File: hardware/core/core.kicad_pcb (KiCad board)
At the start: 4 copper layers, 31.3 x 67.7 mm, 32 parts, among them J17 PROG, J18 USB_C_Receptacle_USB2.0_14P, J5 TO_NEXT, J7 TO_NEXT, J8 Conn_02x09_Odd_Even, SW1 RESET, SW2 BOOT, U10 SN74AHCT1G14DCKR, U19 ESP32-S3-MINI-1, U20 AP2112K-3.3TRG1, U21 SN65HVD230DR

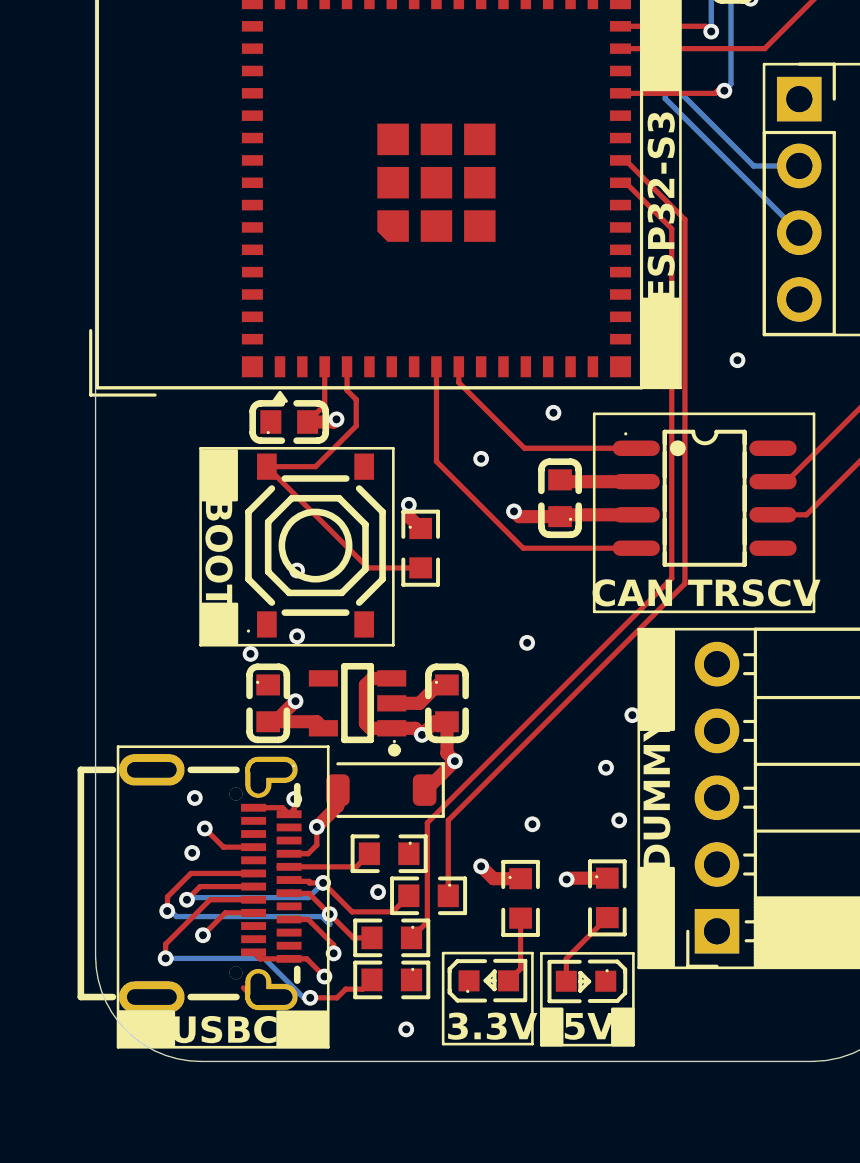
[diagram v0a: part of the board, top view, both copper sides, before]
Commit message: changed schottky with a ss54 and reduced VBUS route length
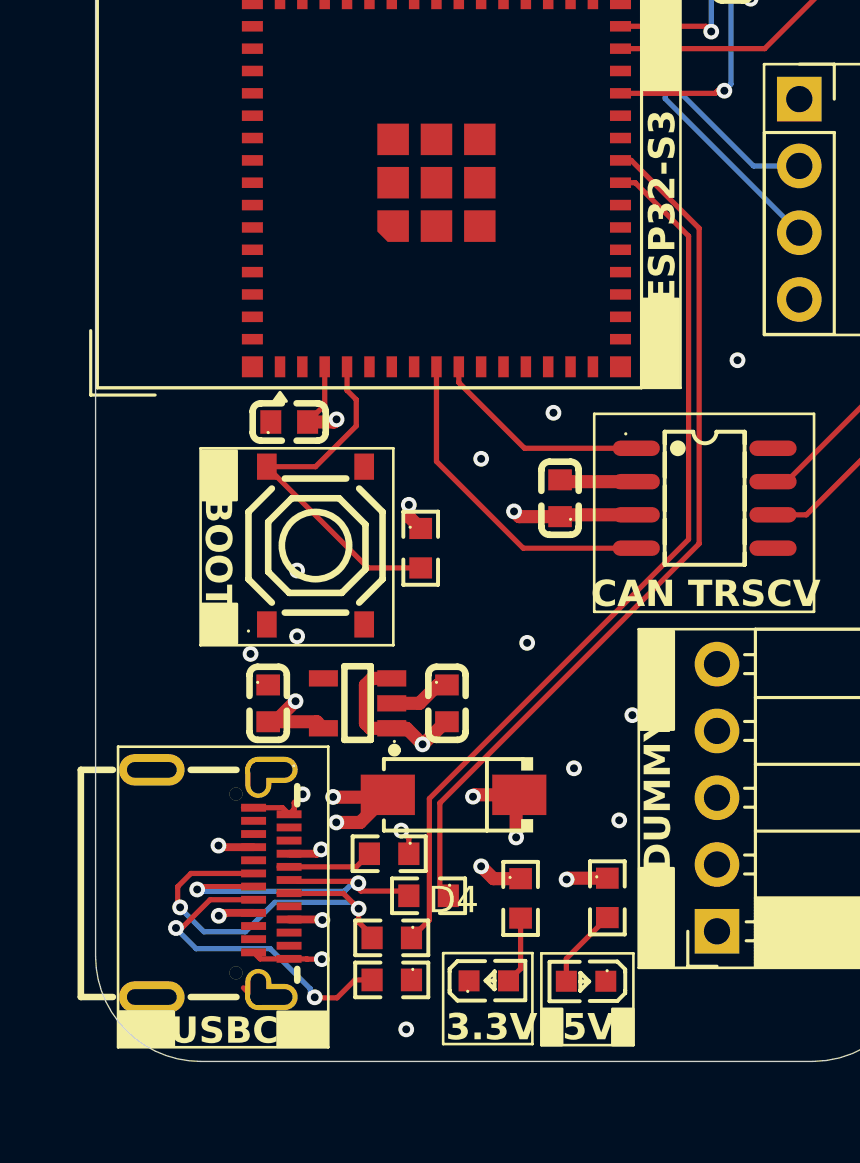
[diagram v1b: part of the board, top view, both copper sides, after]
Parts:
- removed D1: MBR0520LT1G, Diode_SMD:D_SOD-123
- added D4: SS54_C22452, SpaghettiLAB:SMA_L4.4-W2.8-LS5.4-R-RD, F.Cu at (80.7, 125.3)
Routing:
- net Net-(J18-D--PadA7): track 14.9 -> 15.9 mm
- net Net-(J18-CC2): track 13.0 -> 12.0 mm
- net GND: track 13.1 -> 14.1 mm, vias 26 -> 23
- net USB_D+: track 32.8 -> 33.7 mm
- net USB_D-: track 33.7 -> 34.5 mm
- net 5V: track 22.1 -> 22.4 mm, vias 5 -> 6
- net VBUS: track 10.5 -> 10.3 mm, vias 4 -> 6

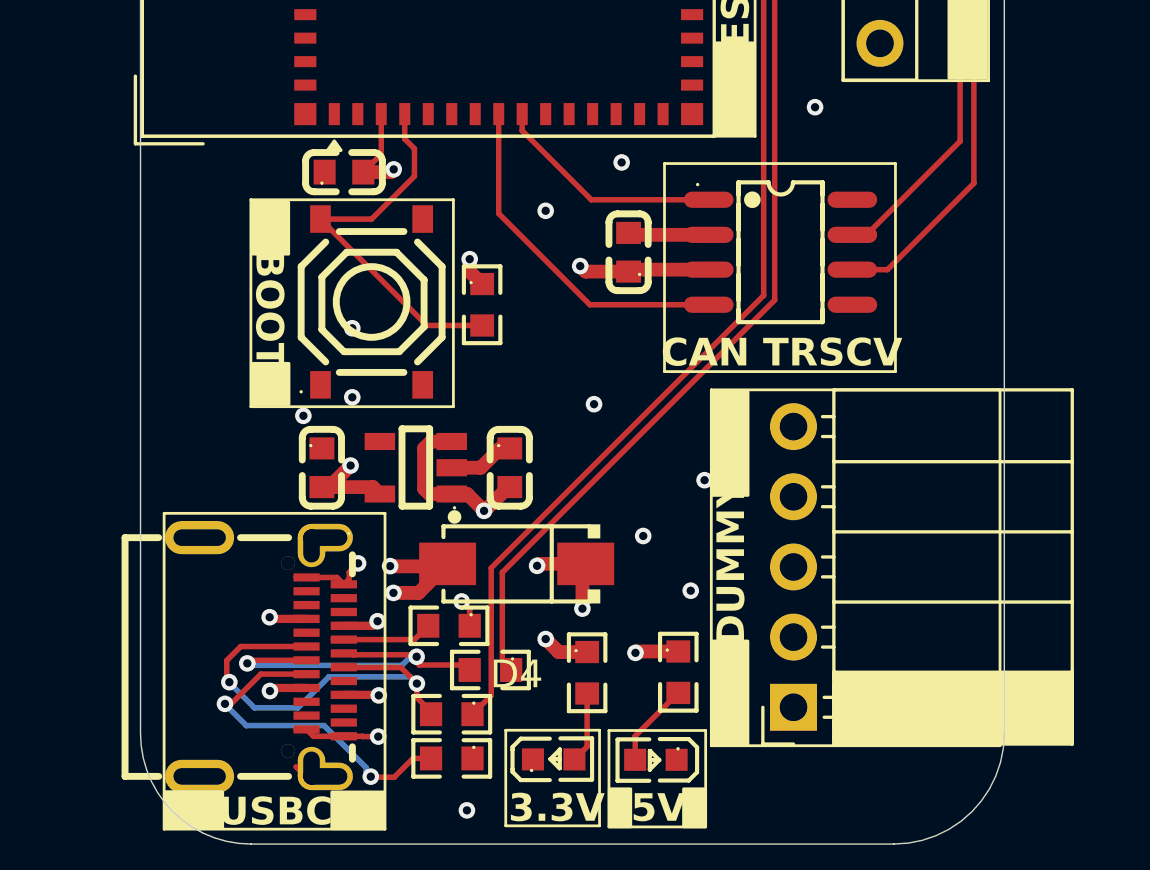
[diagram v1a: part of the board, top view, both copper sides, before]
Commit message: minor fixes to silkscreen, added rev a
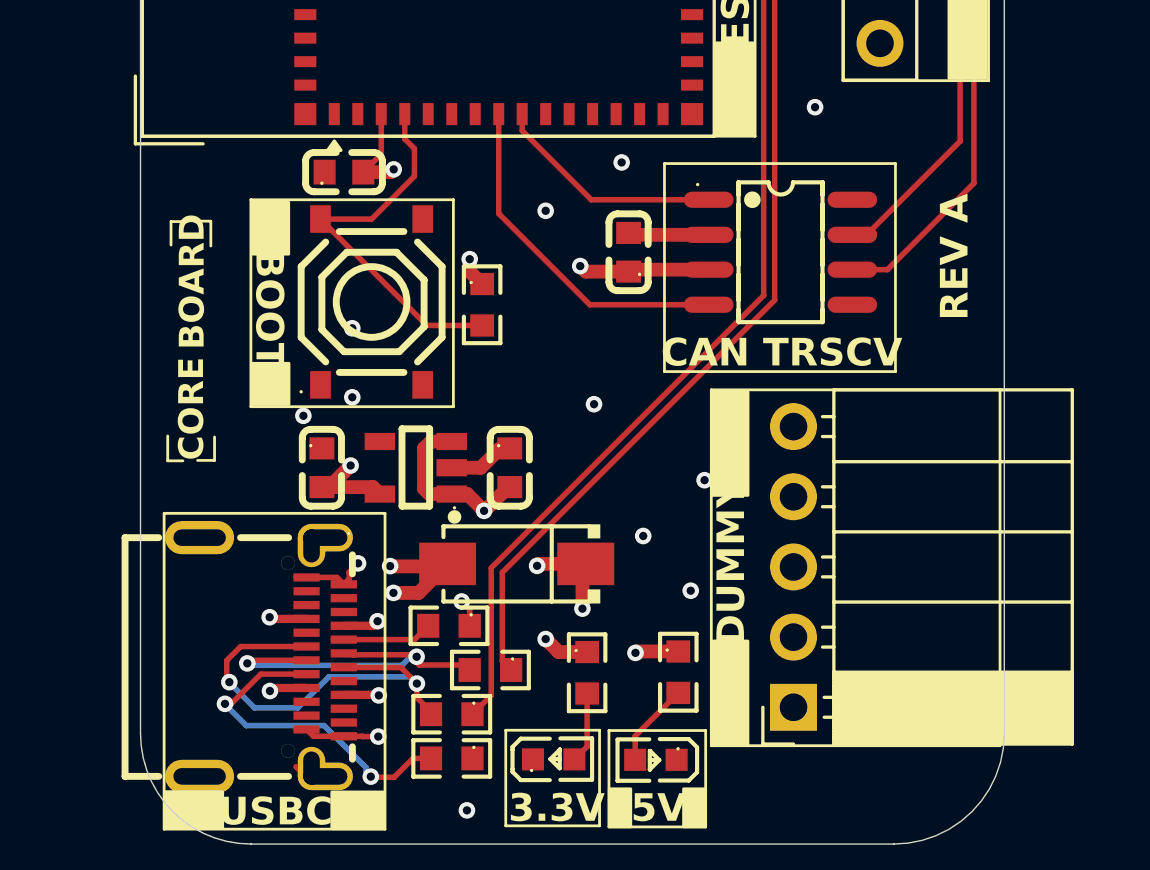
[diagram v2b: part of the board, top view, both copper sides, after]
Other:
- board text added: "BOARD"
- board text added: "CORE"
- board text added: "REV A"
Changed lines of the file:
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@@
 			(at 0 -4 0)
 			(layer "F.SilkS")
+			(hide yes)
 			(effects
 				(font
@@
 				(font
 					(size 1.27 1.27)
+					(thickness 0.15)
 				)
 			)
@@
 		(layer "F.SilkS")
 	)
+	(gr_line
+		(start 68.07 121.55)
+		(end 68.07 120.65)
+		(stroke
+			(width 0.1)
+			(type default)
+		)
+		(layer "F.SilkS")
+	)
+	(gr_line
+		(start 68.19 112.89)
+		(end 68.74 112.89)
+		(stroke
+			(width 0.1)
+			(type default)
+		)
+		(layer "F.SilkS")
+	)
+	(gr_line
+		(start 68.19 113.74)
+		(end 68.19 112.89)
+		(stroke
+			(width 0.1)
+			(type default)
+		)
+		(layer "F.SilkS")
+	)
+	(gr_line
+		(start 68.62 121.55)
+		(end 68.07 121.55)
+		(stroke
+			(width 0.1)
+			(type default)
+		)
+		(layer "F.SilkS")
+	)
+	(gr_line
+		(start 69.08 112.875)
+		(end 69.63 112.875)
+		(stroke
+			(width 0.1)
+			(type default)
+		)
+		(layer "F.SilkS")
+	)
+	(gr_line
+		(start 69.63 112.875)
+		(end 69.63 113.775)
+		(stroke
+			(width 0.1)
+			(type default)
+		)
+		(layer "F.SilkS")
+	)
+	(gr_line
+		(start 69.765 120.685)
+		(end 69.765 121.535)
+		(stroke
+			(width 0.1)
+			(type default)
+		)
+		(layer "F.SilkS")
+	)
+	(gr_line
+		(start 69.765 121.535)
+		(end 69.15 121.535)
+		(stroke
+			(width 0.1)
+			(type default)
+		)
+		(layer "F.SilkS")
+	)
 	(gr_rect
 		(start 71.08 112.1)
@@
 		)
 	)
+	(gr_text "CORE"
+		(at 69.4575 121.535 90)
+		(layer "F.SilkS" knockout)
+		(effects
+			(font
+				(size 0.9 0.9)
+				(thickness 0.2)
+				(bold yes)
+			)
+			(justify left bottom)
+		)
+	)
+	(gr_text "BOARD"
+		(at 69.48 117.525 90)
+		(layer "F.SilkS")
+		(effects
+			(font
+				(size 0.9 0.9)
+				(thickness 0.2)
+				(bold yes)
+			)
+			(justify left bottom)
+		)
+	)
 	(gr_text "3.3V"
 		(at 80.4 134.7 0)
@@
 		)
 	)
+	(gr_text "REV A"
+		(at 97.14 116.47 90)
+		(layer "F.SilkS" knockout)
+		(effects
+			(font
+				(size 1 1)
+				(bold yes)
+			)
+			(justify left bottom)
+		)
+	)
 	(gr_text "LINK BAY"
 		(at 67.36 93 0)
@@
 	)
 	(segment
+		(start 83.25 131.895)
+		(end 83.25 129.97)
+		(width 0.2)
+		(layer "F.Cu")
+		(net "Net-(D2-A)")
+	)
+	(segment
+		(start 82.79 132.355)
+		(end 83.25 131.895)
+		(width 0.2)
+		(layer "F.Cu")
+		(net "Net-(D2-A)")
+	)
+	(segment
+		(start 77 128.02)
+		(end 77.5 127.52)
+		(width 0.2)
+		(layer "F.Cu")
+		(net "Net-(J18-CC1)")
+	)
+	(segment
+		(start 74.06 128.02)
+		(end 77 128.02)
+		(width 0.2)
+		(layer "F.Cu")
+		(net "Net-(J18-CC1)")
+	)
+	(segment
 		(start 77.15 126.33)
 		(end 78.2 125.28)
@@
 	)
 	(segment
-		(start 83.25 131.895)
-		(end 83.25 129.97)
-		(width 0.2)
-		(layer "F.Cu")
-		(net "Net-(D2-A)")
-	)
-	(segment
-		(start 82.79 132.355)
-		(end 83.25 131.895)
-		(width 0.2)
-		(layer "F.Cu")
-		(net "Net-(D2-A)")
-	)
-	(segment
-		(start 77 128.02)
-		(end 77.5 127.52)
-		(width 0.2)
-		(layer "F.Cu")
-		(net "Net-(J18-CC1)")
-	)
-	(segment
-		(start 74.06 128.02)
-		(end 77 128.02)
-		(width 0.2)
-		(layer "F.Cu")
-		(net "Net-(J18-CC1)")
-	)
-	(segment
